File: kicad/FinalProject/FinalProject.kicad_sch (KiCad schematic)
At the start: 10 parts, among them IC1 MIC_I2S_SPH0645, U3 MPU-6050

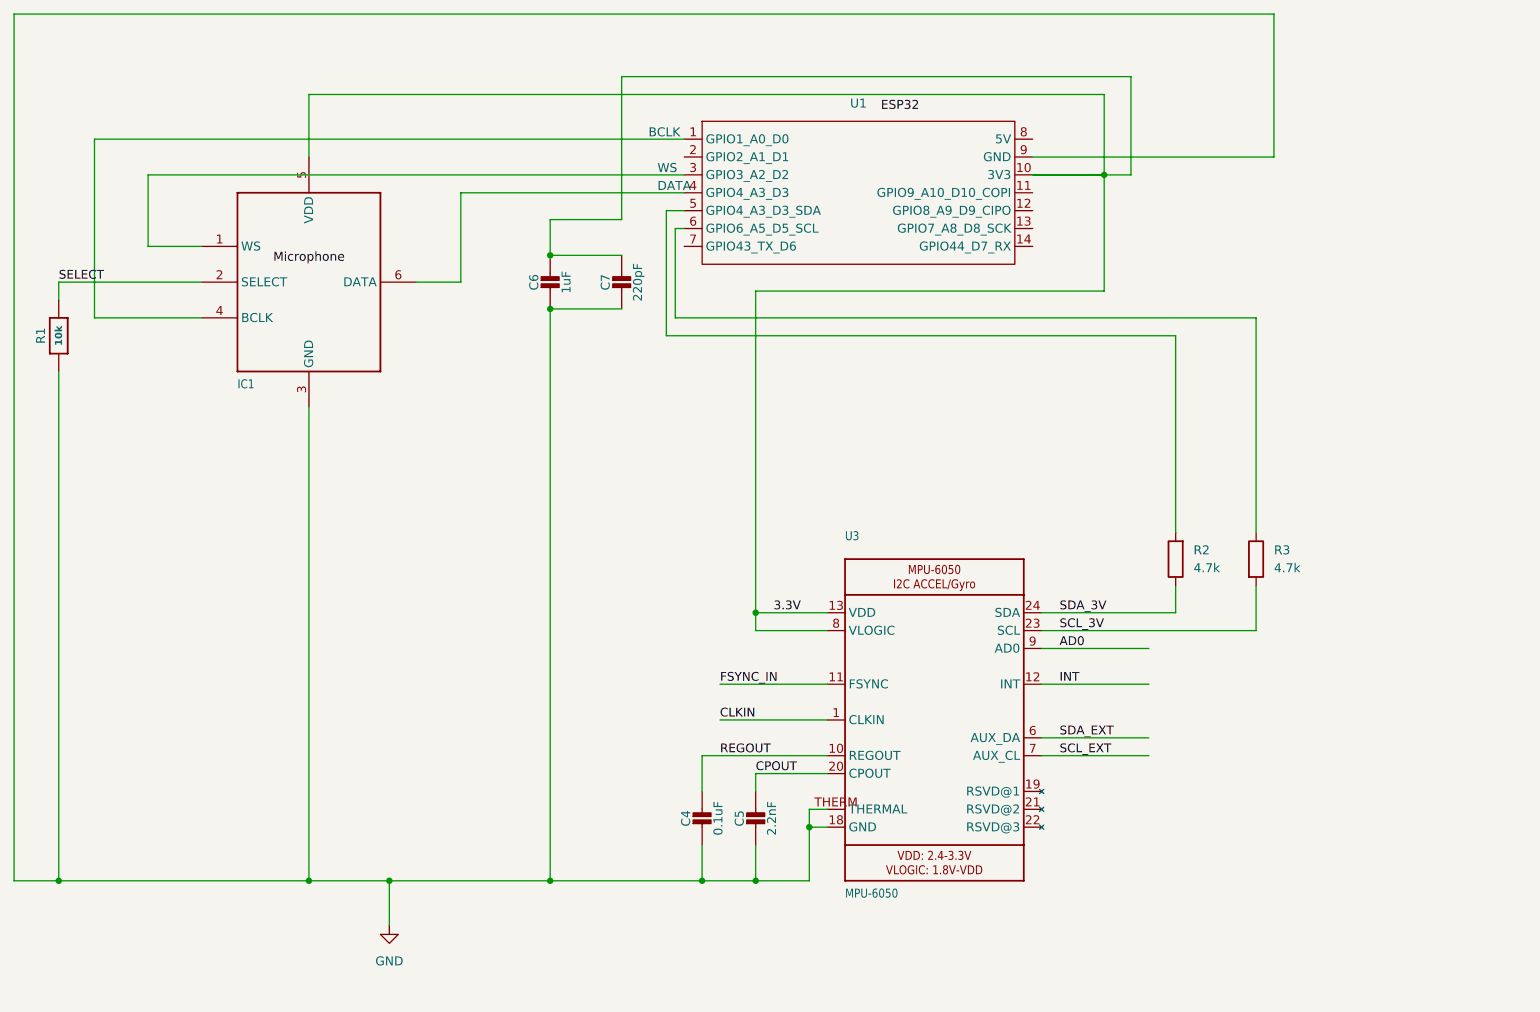
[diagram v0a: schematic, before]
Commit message: added datasheets for led and stepper motor
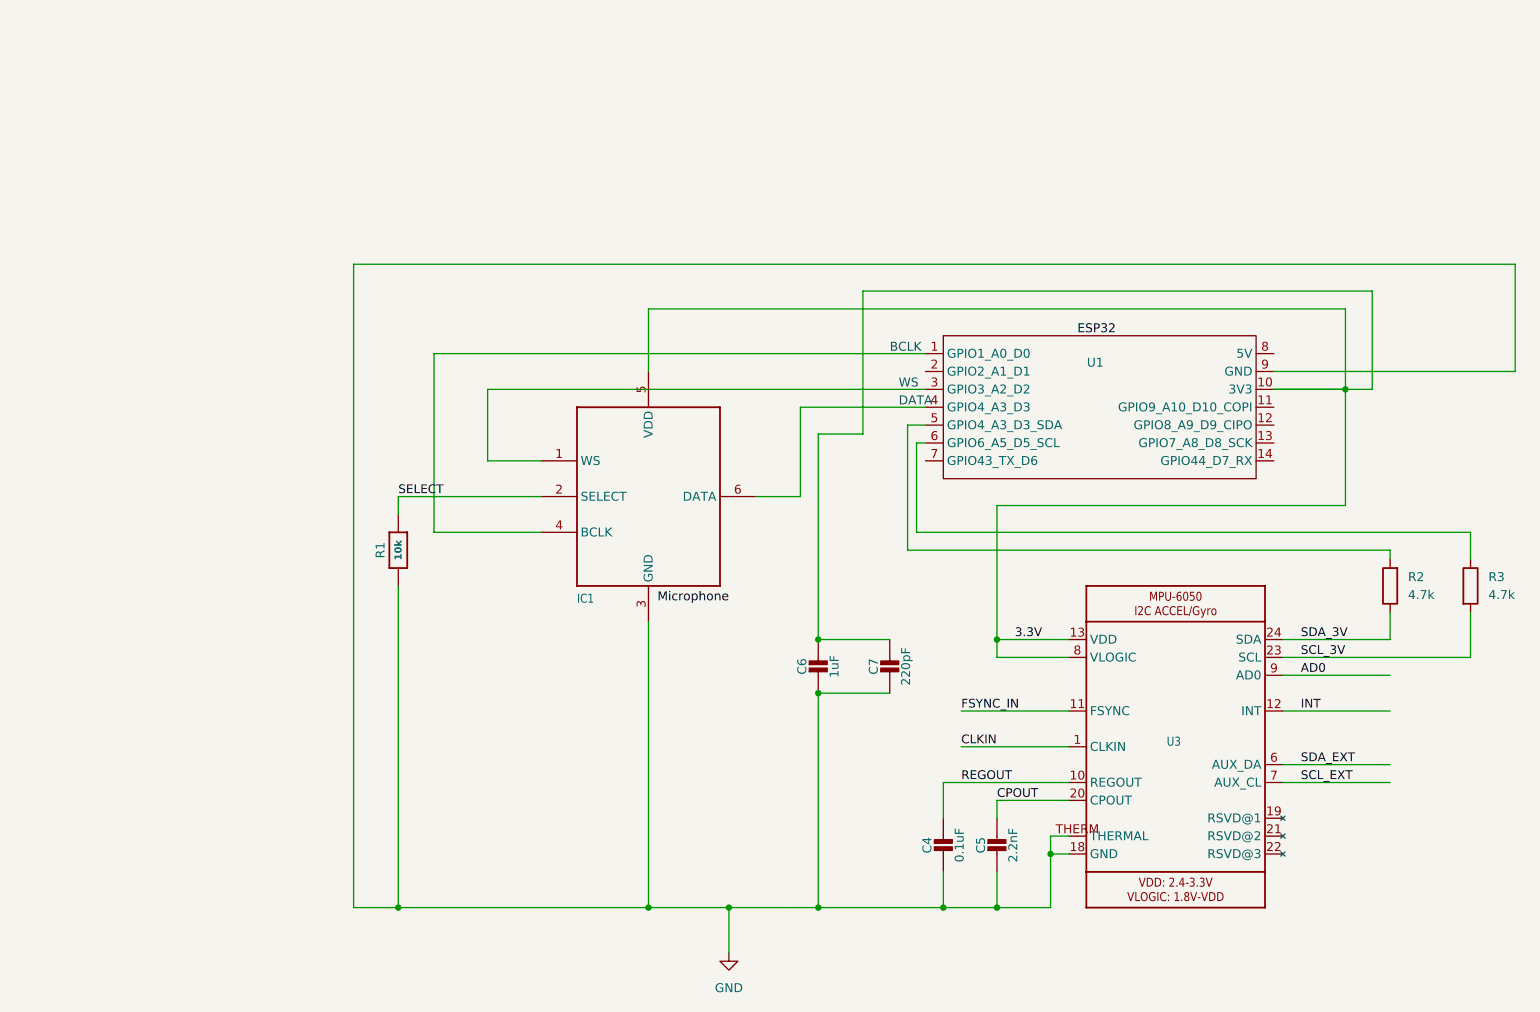
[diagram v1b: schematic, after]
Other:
- moved on the sheet: C4, C5, C6, C7, IC1, R1, R2, R3, U1, U3
